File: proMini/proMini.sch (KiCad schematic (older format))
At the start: 6 parts

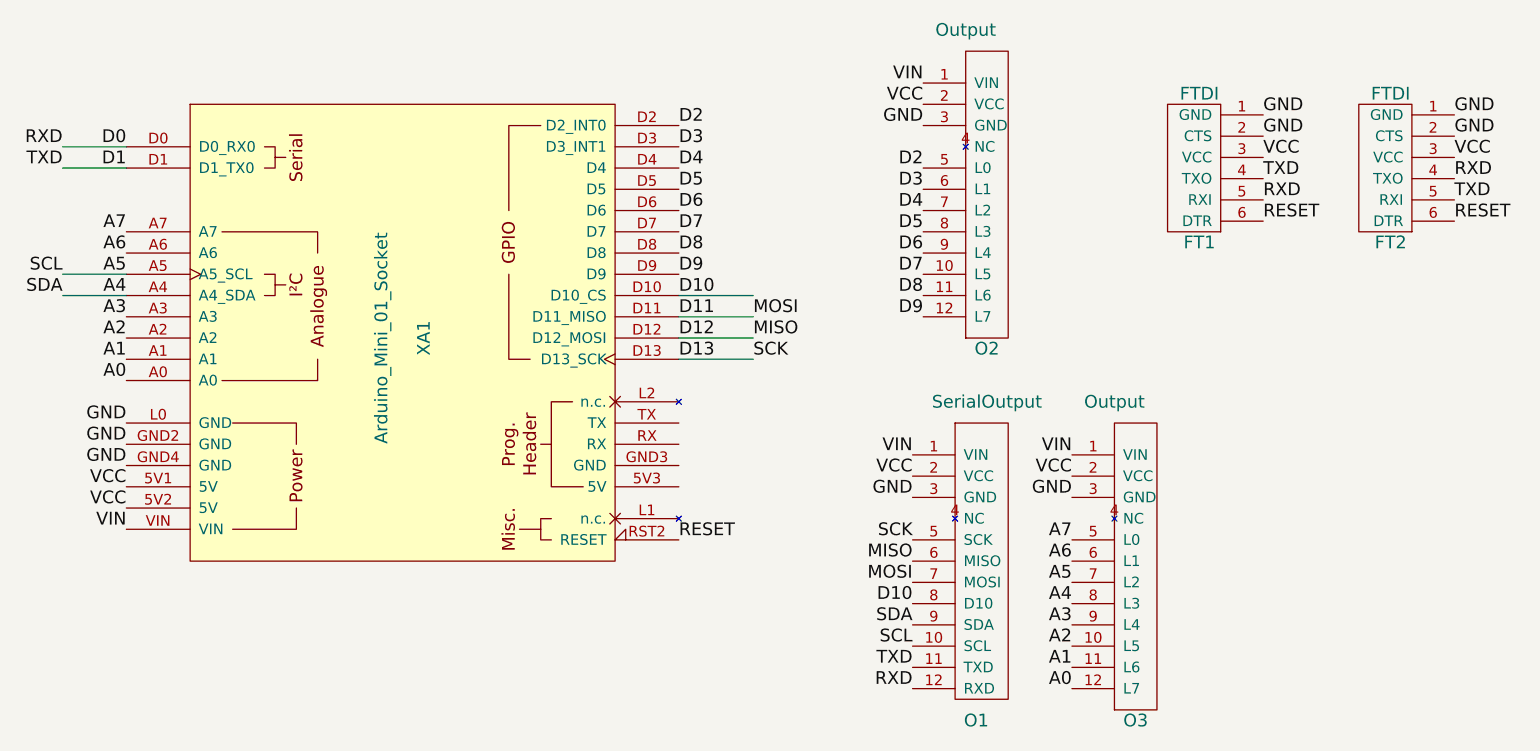
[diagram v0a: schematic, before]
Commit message: More update to make the libraryies use only relative paths.
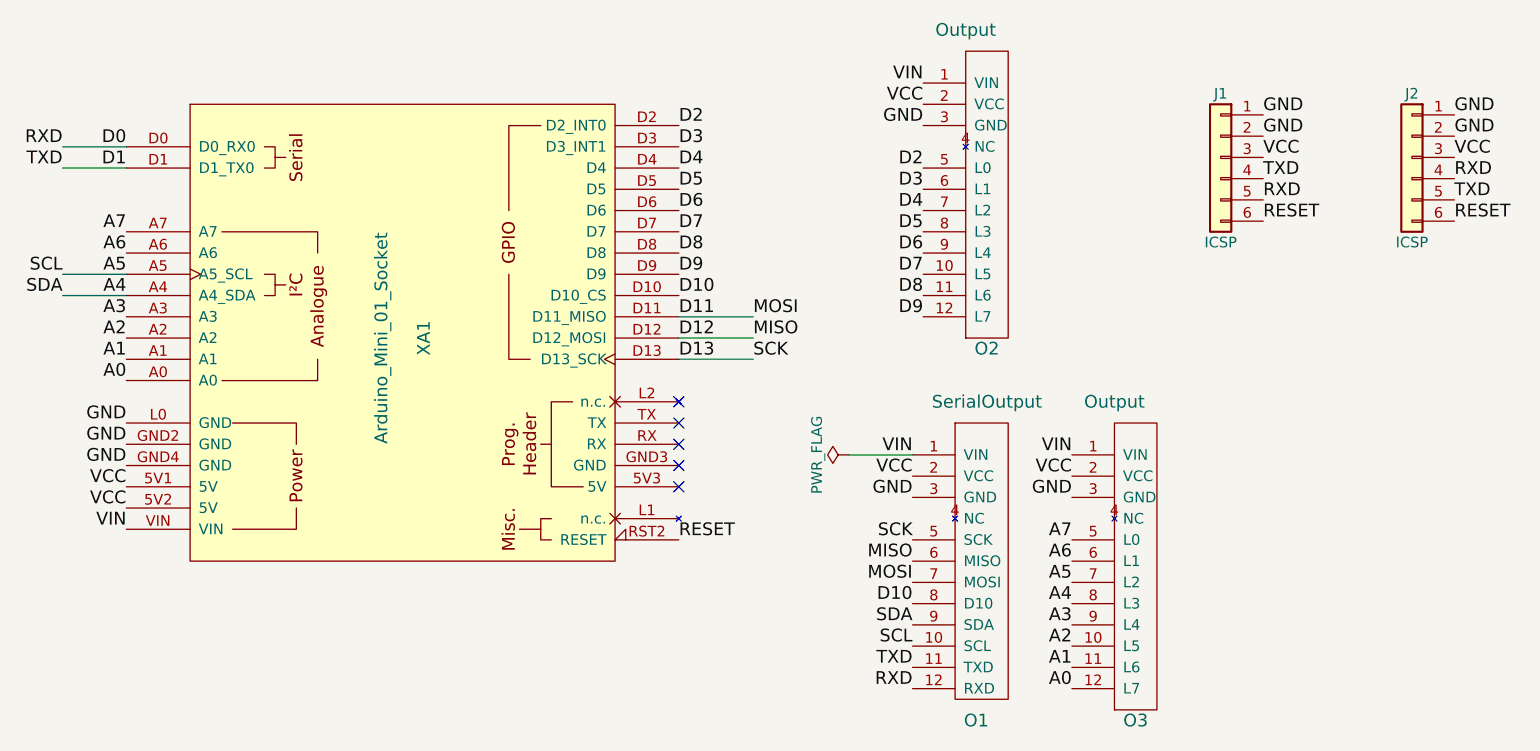
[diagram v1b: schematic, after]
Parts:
- removed FT1, FT2: FTDI, Pin_Headers:Pin_Header_Straight_1x06_Pitch2.54mm, symbol FTDI
- added J1, J2: ICSP, Pin_Headers:Pin_Header_Straight_1x06_Pitch2.54mm, symbol Conn_01x06
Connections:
- no-connect marks 0 -> 5
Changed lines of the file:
@@
 D13
-Wire Wire Line
-	4200 2450 4550 2450
 Wire Wire Line
 	4200 2550 4550 2550
@@
 Text Label 1600 3450 2    60   ~ 0
 VCC
-$Comp
-L FTDI FT1
-U 1 1 5AE78A82
-P 6650 1850
-F 0 "FT1" H 6650 1500 60  0000 C CNN
-F 1 "FTDI" H 6650 2200 60  0000 C CNN
-F 2 "Pin_Headers:Pin_Header_Straight_1x06_Pitch2.54mm" H 6650 1850 60  0001 C CNN
-F 3 "" H 6650 1850 60  0001 C CNN
-	1    6650 1850
-	1    0    0    -1
-$EndComp
 Text Label 6950 1600 0    60   ~ 0
 GND
@@
 Text Label 4200 3600 0    60   ~ 0
 RESET
-$Comp
-L FTDI FT2
-U 1 1 5AE78D08
-P 7550 1850
-F 0 "FT2" H 7550 1500 60  0000 C CNN
-F 1 "FTDI" H 7550 2200 60  0000 C CNN
-F 2 "Pin_Headers:Pin_Header_Straight_1x06_Pitch2.54mm" H 7550 1850 60  0001 C CNN
-F 3 "" H 7550 1850 60  0001 C CNN
-	1    7550 1850
-	1    0    0    -1
-$EndComp
 Text Label 7850 1600 0    60   ~ 0
 GND
@@
 Text Label 7850 2100 0    60   ~ 0
 RESET
+$Comp
+L Conn_01x06 J1
+U 1 1 5AFEF05A
+P 6750 1800
+F 0 "J1" H 6750 2100 50  0000 C CNN
+F 1 "ICSP" H 6750 1400 50  0000 C CNN
+F 2 "Pin_Headers:Pin_Header_Straight_1x06_Pitch2.54mm" H 6750 1800 50  0001 C CNN
+F 3 "" H 6750 1800 50  0001 C CNN
+	1    6750 1800
+	-1   0    0    -1
+$EndComp
+$Comp
+L Conn_01x06 J2
+U 1 1 5AFEF100
+P 7650 1800
+F 0 "J2" H 7650 2100 50  0000 C CNN
+F 1 "ICSP" H 7650 1400 50  0000 C CNN
+F 2 "Pin_Headers:Pin_Header_Straight_1x06_Pitch2.54mm" H 7650 1800 50  0001 C CNN
+F 3 "" H 7650 1800 50  0001 C CNN
+	1    7650 1800
+	-1   0    0    -1
+$EndComp
+$Comp
+L PWR_FLAG #FLG01
+U 1 1 5AFEF1E7
+P 5000 3200
+F 0 "#FLG01" H 5000 3275 50  0001 C CNN
+F 1 "PWR_FLAG" H 5000 3350 50  0000 C CNN
+F 2 "" H 5000 3200 50  0001 C CNN
+F 3 "" H 5000 3200 50  0001 C CNN
+	1    5000 3200
+	0    -1   -1   0
+$EndComp
+Wire Wire Line
+	5000 3200 5300 3200
+NoConn ~ 4200 2950
+NoConn ~ 4200 3050
+NoConn ~ 4200 3150
+NoConn ~ 4200 3250
+NoConn ~ 4200 3350
 $EndSCHEMATC
